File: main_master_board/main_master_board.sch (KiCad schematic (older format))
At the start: 4 parts, among them P5 Mounting Holes, P6 Mounting Holes, P7 Mounting Holes, P8 Mounting Holes

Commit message: Cleaned up some wires and moved connectors out to main page. Also added some LEDs
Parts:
- added D1, D2: D_Schottky, TO-220-3:D-Pack-3, symbol D_Schottky
- added D3: P6SMB30AT3G, Diodes_SMD:SMB_Standard, symbol ZENERsmall
- added F1: 3413.0328.22, dp_devices:dp_devices-C1206, symbol Fuse
- added P1: Hebi_1, Connectors_Molex:Molex_MiniFit-JR-5556-02A_2x01x4.20mm_Straight, symbol CONN_01X02
- added P13: CONN_02X15, symbol CONN_02X15
- added P2: Hebi_2, Connectors_Molex:Molex_MiniFit-JR-5556-02A_2x01x4.20mm_Straight, symbol CONN_01X02
- added P3: Vbackup, microclasp:microclasp_2, symbol CONN_01X02
- added P4: CONN_02X05, Connectors_Molex:Molex_NanoFit_2x05x2.50mm_Straight, symbol CONN_02X05
- added S1: SWITCH_DPDT, microclasp:microclasp_3, symbol SWITCH_DPDT
- added SW1: SWITCH_SPST, microclasp:microclasp_2, symbol SWITCH_SPST
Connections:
- net labels added: KS_physical_in, KS_physical_out, Switch_on, V24_in, V4, V_hebi1, V_hebi2, signal_1s, signal_2s, signal_3s, signal_4s, signal_5s, signal_6s, uC_GPIO1, uC_GPIO2
- net labels removed: +12V, +1V8, V12
- wire segments 79 -> 119
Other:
- note added: "Bettery Reverse\nCurrent Protection"
- note added: "Circuits can take 48V, \nexcept TSV diode"
- note added: "Manual switch to \nturn motors off"
- note added: "Molex Nano-Fit"
- note added: "Transient Voltage Suppessor"

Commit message: Started routing! 24 to 5 buck
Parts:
- D1, D2: footprint TO-220-3:D-Pack-3 -> PowerDI:PowerDI
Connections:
- wire segments 119 -> 111
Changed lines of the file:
@@
 LIBS:Sensors
 LIBS:LP3852-3.3
-LIBS:0s102011ma1qn1
-LIBS:74LVC1G17
-LIBS:74V1T126
-LIBS:acs711klctr-12ab-t
-LIBS:AD7192
-LIBS:AD7193
-LIBS:am-hrr30-xxx
-LIBS:aon7528
-LIBS:AP7363
-LIBS:AS1359
-LIBS:csd16323q3
-LIBS:dmn2004dmk
-LIBS:dp_devices
-LIBS:DSPIC33E128MC506
-LIBS:fds6898az
-LIBS:ina197
-LIBS:irf7329pbf
-LIBS:ld1117
-LIBS:lm3478
-LIBS:lm3481
-LIBS:lt1910
-LIBS:ltc1871
-LIBS:ltc1982
-LIBS:MAG3110
-LIBS:mcp1700
-LIBS:mcp73831
-LIBS:mcsmt-g5030a1-3712
-LIBS:microchip_can
-LIBS:microclasp_hdrx2
-LIBS:microclasp_hdrx3
-LIBS:MPU-6000_MPU-6050
-LIBS:MPU-9150
-LIBS:nrf24l01+
-LIBS:pds1040l
-LIBS:pic12f1571
-LIBS:pinhead
-LIBS:psmn013-80ys
-LIBS:RESISTOR_ARRAY
-LIBS:rf803d
-LIBS:RGB_LED
-LIBS:Si1970DH
-LIBS:sn65hvd232
-LIBS:ssc54
-LIBS:sw_push_4
-LIBS:tc74
-LIBS:TPS2113A
-LIBS:tps54540
-LIBS:vs-mbrb1635pbf
-LIBS:xal5050-562meb
-LIBS:xal6030-182mec
+LIBS:decaWave
 LIBS:conn_2x50
 LIBS:conn_open_q_x2
@@
 LIBS:ac-dc
 LIBS:actel
+LIBS:allegro
 LIBS:Altera
 LIBS:analog_devices
@@
 LIBS:logo
 LIBS:maxim
+LIBS:mechanical
 LIBS:microchip_dspic33dsc
 LIBS:microchip_pic10mcu
@@
 LIBS:microchip_pic32mcu
 LIBS:motor_drivers
+LIBS:motors
 LIBS:msp430
 LIBS:nordicsemi
@@
 LIBS:ttl_ieee
 LIBS:video
+LIBS:wiznet
 LIBS:Worldsemi
 LIBS:Xicor
+LIBS:zetex
 LIBS:Zilog
 LIBS:conn_2x45
@@
 Comment4 ""
 $EndDescr
-$Comp
-L +3V3 #PWR01
-U 1 1 58094C11
-P 1360 690
-F 0 "#PWR01" H 1360 540 50  0001 C CNN
-F 1 "+3V3" H 1360 830 50  0000 C CNN
-F 2 "" H 1360 690 50  0000 C CNN
-F 3 "" H 1360 690 50  0000 C CNN
-	1    1360 690
-	1    0    0    -1
-$EndComp
-$Comp
-L GND #PWR02
-U 1 1 58094D2E
-P 1250 1200
-F 0 "#PWR02" H 1250 950 50  0001 C CNN
-F 1 "GND" H 1250 1050 50  0000 C CNN
-F 2 "" H 1250 1200 50  0000 C CNN
-F 3 "" H 1250 1200 50  0000 C CNN
-	1    1250 1200
-	1    0    0    -1
-$EndComp
-$Comp
-L +24V #PWR03
-U 1 1 58643E79
-P 870 700
-F 0 "#PWR03" H 870 550 50  0001 C CNN
-F 1 "+24V" H 870 840 50  0000 C CNN
-F 2 "" H 870 700 50  0000 C CNN
-F 3 "" H 870 700 50  0000 C CNN
-	1    870  700
-	1    0    0    -1
-$EndComp
-$Comp
-L +5V #PWR04
-U 1 1 586440F8
-P 1120 690
-F 0 "#PWR04" H 1120 540 50  0001 C CNN
-F 1 "+5V" H 1120 830 50  0000 C CNN
-F 2 "" H 1120 690 50  0000 C CNN
-F 3 "" H 1120 690 50  0000 C CNN
-	1    1120 690
-	1    0    0    -1
-$EndComp
 $Sheet
 S 4700 860  1110 1660
@@
 Text Label 6965 1025 0    60   ~ 0
 Vmain
-$Comp
-L PWR_FLAG #FLG05
-U 1 1 58713441
-P 1120 1140
-F 0 "#FLG05" H 1120 1235 50  0001 C CNN
-F 1 "PWR_FLAG" H 1120 1320 50  0000 C CNN
-F 2 "" H 1120 1140 50  0000 C CNN
-F 3 "" H 1120 1140 50  0000 C CNN
-	1    1120 1140
-	1    0    0    -1
-$EndComp
-$Comp
-L PWR_FLAG #FLG06
-U 1 1 5871371D
-P 1120 790
-F 0 "#FLG06" H 1120 885 50  0001 C CNN
-F 1 "PWR_FLAG" H 1120 970 50  0001 C CNN
-F 2 "" H 1120 790 50  0000 C CNN
-F 3 "" H 1120 790 50  0000 C CNN
-	1    1120 790
-	-1   0    0    1
-$EndComp
-$Comp
-L GNDPWR #PWR07
-U 1 1 58714A82
-P 960 1200
-F 0 "#PWR07" H 960 1000 50  0001 C CNN
-F 1 "GNDPWR" H 960 1070 50  0000 C CNN
-F 2 "" H 960 1150 50  0000 C CNN
-F 3 "" H 960 1150 50  0000 C CNN
-	1    960  1200
-	1    0    0    -1
-$EndComp
-Text Notes 530  1580 0    60   ~ 0
+Text Notes 505  805  0    60   ~ 0
 Two Grounds to separate \nmotor ground and electronics ground
 Text Label 5850 1210 0    60   ~ 0
@@
 3V3
 $Comp
-L GNDPWR #PWR08
+L GNDPWR #PWR01
 U 1 1 58756896
 P 4460 2550
-F 0 "#PWR08" H 4460 2350 50  0001 C CNN
+F 0 "#PWR01" H 4460 2350 50  0001 C CNN
 F 1 "GNDPWR" H 4460 2420 50  0000 C CNN
 F 2 "" H 4460 2500 50  0000 C CNN
@@
 $EndComp
 $Comp
-L GND #PWR09
+L GND #PWR02
 U 1 1 58756928
 P 6030 2540
-F 0 "#PWR09" H 6030 2290 50  0001 C CNN
+F 0 "#PWR02" H 6030 2290 50  0001 C CNN
 F 1 "GND" H 6030 2390 50  0000 C CNN
 F 2 "" H 6030 2540 50  0000 C CNN
@@
 Vmotors
 $Comp
-L GND #PWR010
+L GND #PWR03
 U 1 1 5875B134
 P 7125 1915
-F 0 "#PWR010" H 7125 1665 50  0001 C CNN
+F 0 "#PWR03" H 7125 1665 50  0001 C CNN
 F 1 "GND" H 7125 1765 50  0000 C CNN
 F 2 "" H 7125 1915 50  0000 C CNN
@@
 $EndComp
 $Comp
-L GNDPWR #PWR011
+L GNDPWR #PWR04
 U 1 1 5875E5EF
 P 6875 1935
-F 0 "#PWR011" H 6875 1735 50  0001 C CNN
+F 0 "#PWR04" H 6875 1735 50  0001 C CNN
 F 1 "GNDPWR" H 6875 1805 50  0000 C CNN
 F 2 "" H 6875 1885 50  0000 C CNN
@@
 $EndSheet
 $Comp
-L GND #PWR012
+L GND #PWR05
 U 1 1 587B1461
 P 11140 940
-F 0 "#PWR012" H 11140 690 50  0001 C CNN
+F 0 "#PWR05" H 11140 690 50  0001 C CNN
 F 1 "GND" H 11140 790 50  0000 C CNN
 F 2 "" H 11140 940 50  0000 C CNN
@@
 prog_tx
 $Comp
-L GND #PWR013
+L GND #PWR06
 U 1 1 588455B7
 P 7955 6190
-F 0 "#PWR013" H 7955 5940 50  0001 C CNN
+F 0 "#PWR06" H 7955 5940 50  0001 C CNN
 F 1 "GND" H 7955 6040 50  0000 C CNN
 F 2 "" H 7955 6190 50  0000 C CNN
@@
 sensor_SCL
 Wire Wire Line
-	1120 690  1120 790
-Wire Wire Line
 	4700 1210 4150 1210
 Wire Wire Line
@@
 Wire Wire Line
 	6945 1025 7235 1025
-Wire Wire Line
-	870  700  870  750
-Wire Wire Line
-	870  750  1360 750
-Connection ~ 1120 750
-Wire Wire Line
-	1360 750  1360 690
-Wire Wire Line
-	960  1200 960  1140
-Wire Wire Line
-	960  1140 1250 1140
-Wire Wire Line
-	1250 1140 1250 1200
-Connection ~ 1120 1140
 Wire Wire Line
 	5810 1210 6075 1210
@@
 	5675 4860 6225 4860
 $Comp
-L GND #PWR014
+L GND #PWR07
 U 1 1 5889E95F
 P 4125 5785
-F 0 "#PWR014" H 4125 5535 50  0001 C CNN
+F 0 "#PWR07" H 4125 5535 50  0001 C CNN
 F 1 "GND" H 4125 5635 50  0000 C CNN
 F 2 "" H 4125 5785 50  0000 C CNN
@@
 Vbackup_in
 $Comp
-L GND #PWR015
+L GND #PWR08
 U 1 1 588D5080
 P 1480 5060
-F 0 "#PWR015" H 1480 4810 50  0001 C CNN
+F 0 "#PWR08" H 1480 4810 50  0001 C CNN
 F 1 "GND" H 1480 4910 50  0000 C CNN
 F 2 "" H 1480 5060 50  0000 C CNN
@@
 V_hebi1
 $Comp
-L GNDPWR #PWR016
+L GNDPWR #PWR09
 U 1 1 588D5095
 P 1185 5830
-F 0 "#PWR016" H 1185 5630 50  0001 C CNN
+F 0 "#PWR09" H 1185 5630 50  0001 C CNN
 F 1 "GNDPWR" H 1185 5700 50  0000 C CNN
 F 2 "" H 1185 5780 50  0000 C CNN
@@
 $EndComp
 $Comp
-L GNDPWR #PWR017
+L GNDPWR #PWR010
 U 1 1 588D509B
 P 1175 6270
-F 0 "#PWR017" H 1175 6070 50  0001 C CNN
+F 0 "#PWR010" H 1175 6070 50  0001 C CNN
 F 1 "GNDPWR" H 1175 6140 50  0000 C CNN
 F 2 "" H 1175 6220 50  0000 C CNN
@@
 F 0 "D2" H 1135 7050 50  0000 C CNN
 F 1 "D_Schottky" H 1135 6850 50  0000 C CNN
-F 2 "TO-220-3:D-Pack-3" H 1135 6950 50  0001 C CNN
+F 2 "PowerDI:PowerDI" H 1135 6950 50  0001 C CNN
 F 3 "http://datasheet.octopart.com/STPS5H100B-TR-STMicroelectronics-datasheet-5318140.pdf" H 1135 6950 50  0001 C CNN
 	1    1135 6950
@@
 F 0 "D1" H 1125 7340 50  0000 C CNN
 F 1 "D_Schottky" H 1125 7140 50  0000 C CNN
-F 2 "TO-220-3:D-Pack-3" H 1125 7240 50  0001 C CNN
+F 2 "PowerDI:PowerDI" H 1125 7240 50  0001 C CNN
 F 3 "http://datasheet.octopart.com/STPS5H100B-TR-STMicroelectronics-datasheet-5318140.pdf" H 1125 7240 50  0001 C CNN
 	1    1125 7240
@@
 	1190 3790 1190 3820
 $Comp
-L GNDPWR #PWR018
+L GNDPWR #PWR011
 U 1 1 588D5126
 P 1190 3820
-F 0 "#PWR018" H 1190 3620 50  0001 C CNN
+F 0 "#PWR011" H 1190 3620 50  0001 C CNN
 F 1 "GNDPWR" H 1190 3690 50  0000 C CNN
 F 2 "" H 1190 3770 50  0000 C CNN
@@
 $EndComp
 $Comp
-L GNDPWR #PWR019
+L GNDPWR #PWR012
 U 1 1 588D512C
 P 2030 4420
-F 0 "#PWR019" H 2030 4220 50  0001 C CNN
+F 0 "#PWR012" H 2030 4220 50  0001 C CNN
 F 1 "GNDPWR" H 2030 4290 50  0000 C CNN
 F 2 "" H 2030 4370 50  0000 C CNN
@@
 	8555 1310 9330 1310
 $Comp
-L GNDPWR #PWR020
+L GNDPWR #PWR013
 U 1 1 588EACE1
 P 1320 2845
-F 0 "#PWR020" H 1320 2645 50  0001 C CNN
+F 0 "#PWR013" H 1320 2645 50  0001 C CNN
 F 1 "GNDPWR" H 1320 2715 50  0000 C CNN
 F 2 "" H 1320 2795 50  0000 C CNN
@@
 V4
 $Comp
-L +24V #PWR021
+L +24V #PWR014
 U 1 1 58919C55
 P 4300 900
-F 0 "#PWR021" H 4300 750 50  0001 C CNN
+F 0 "#PWR014" H 4300 750 50  0001 C CNN
 F 1 "+24V" H 4300 1040 50  0000 C CNN
 F 2 "" H 4300 900 50  0000 C CNN
@@
 Switch_on
 $Comp
-L +5V #PWR022
+L +5V #PWR015
 U 1 1 58924C9E
 P 6075 1175
-F 0 "#PWR022" H 6075 1025 50  0001 C CNN
+F 0 "#PWR015" H 6075 1025 50  0001 C CNN
 F 1 "+5V" H 6075 1315 50  0000 C CNN
 F 2 "" H 6075 1175 50  0000 C CNN
@@
 $EndComp
 $Comp
-L +3V3 #PWR023
+L +3V3 #PWR016
 U 1 1 58925954
 P 6075 1425
-F 0 "#PWR023" H 6075 1275 50  0001 C CNN
+F 0 "#PWR016" H 6075 1275 50  0001 C CNN
 F 1 "+3V3" H 6075 1565 50  0000 C CNN
 F 2 "" H 6075 1425 50  0000 C CNN
@@
 Wire Wire Line
 	6075 1460 6075 1425
-$Comp
-L +24V #PWR024
-U 1 1 5892EF1B
-P 600 2425
-F 0 "#PWR024" H 600 2275 50  0001 C CNN
-F 1 "+24V" H 600 2565 50  0000 C CNN
-F 2 "" H 600 2425 50  0000 C CNN
-F 3 "" H 600 2425 50  0000 C CNN
-	1    600  2425
-	1    0    0    -1
-$EndComp
-Wire Wire Line
-	600  2545 600  2425
 $EndSCHEMATC

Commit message: Routing power. Added 5V leveling cap.
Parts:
- removed P13: CONN_02X15, symbol CONN_02X15
- added P13: CONN_02X20, Hirose:DF40HC(3.0)-40DS-0.4V(51), symbol CONN_02X20
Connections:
- net labels added: 1V8, I2C1_SCL, I2C1_SDA, PRTCTL2, PRTCTL3, RB11, RB12, RD1, RD2, RD3, RD4, RD5, RD9, RE5, RF2, RF3, RF4, RF5, RF6, SDC2_CLK, SDC2_CMD, SDC2_DATA_0, SDC2_DATA_1, SDC2_DATA_2, SDC2_DATA_3, UART0_CTS_N, UART0_RTS_N, UART0_RX, UART0_TX, USBDM2, USBDM3, USBDP2, USBDP3, VREG_L11_SDC
- wire segments 111 -> 190
- no-connect marks 0 -> 1
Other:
- moved on the sheet: S1A, SW1

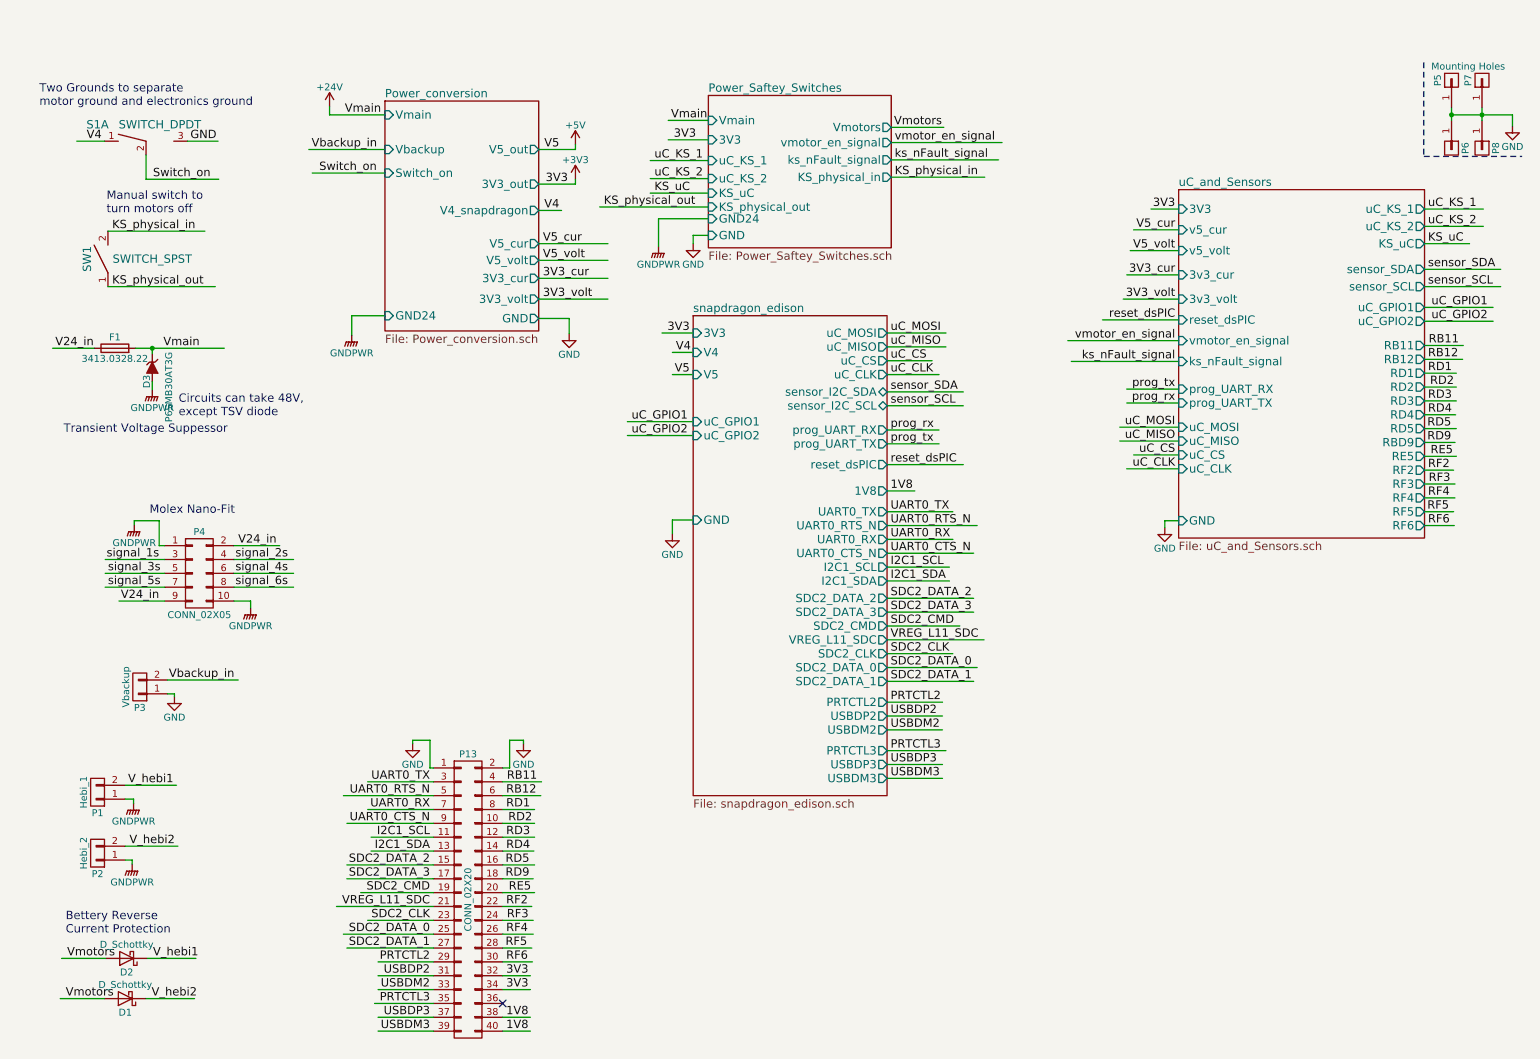
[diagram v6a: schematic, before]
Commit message: Addind support for a push button start and stop
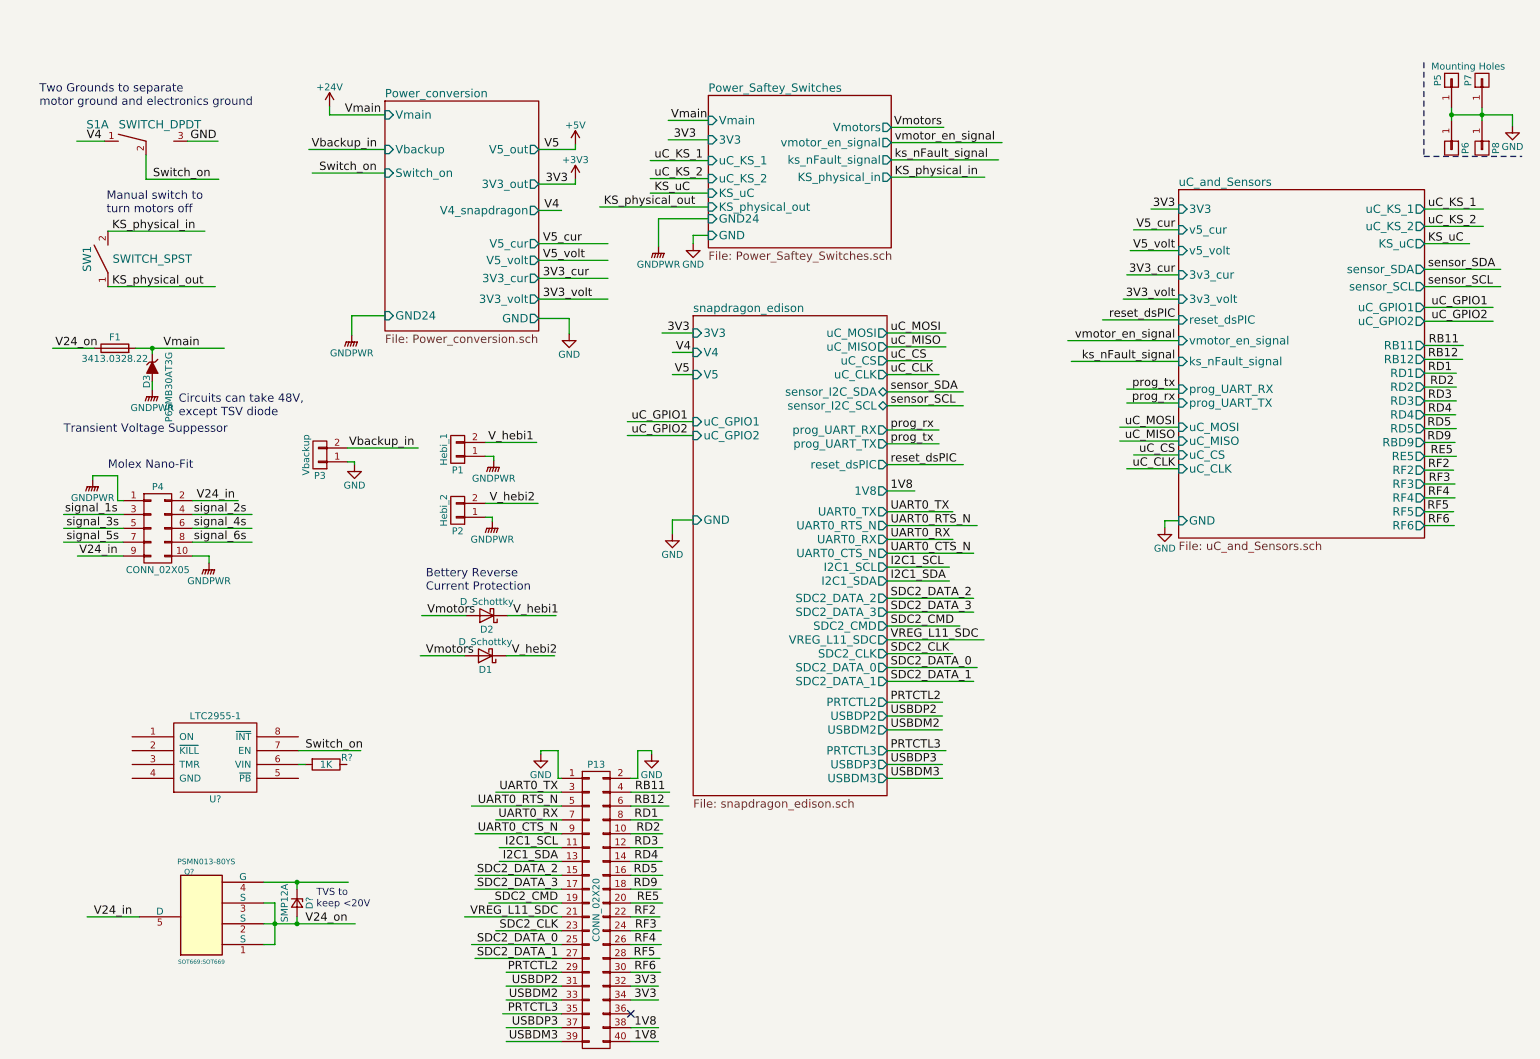
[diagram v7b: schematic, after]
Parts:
- added D?: SMP12A, DO-220AA:DO-220AA, symbol D_Zener_Small
- added Q?: PSMN013-80YS, SOT669:SOT669, symbol PSMN013-80YS
- added R?: 1K, symbol R
- added U?: LTC2955-1, MODULE, symbol LTC2955-1
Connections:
- net labels added: V24_on
- wire segments 190 -> 208
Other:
- note added: "TVS to \nkeep <20V"
- moved on the sheet: D1, D2, P1, P13, P2, P3, P4

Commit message: Working on routing near n-p mosfets. save point incase new apporach doesn't work out
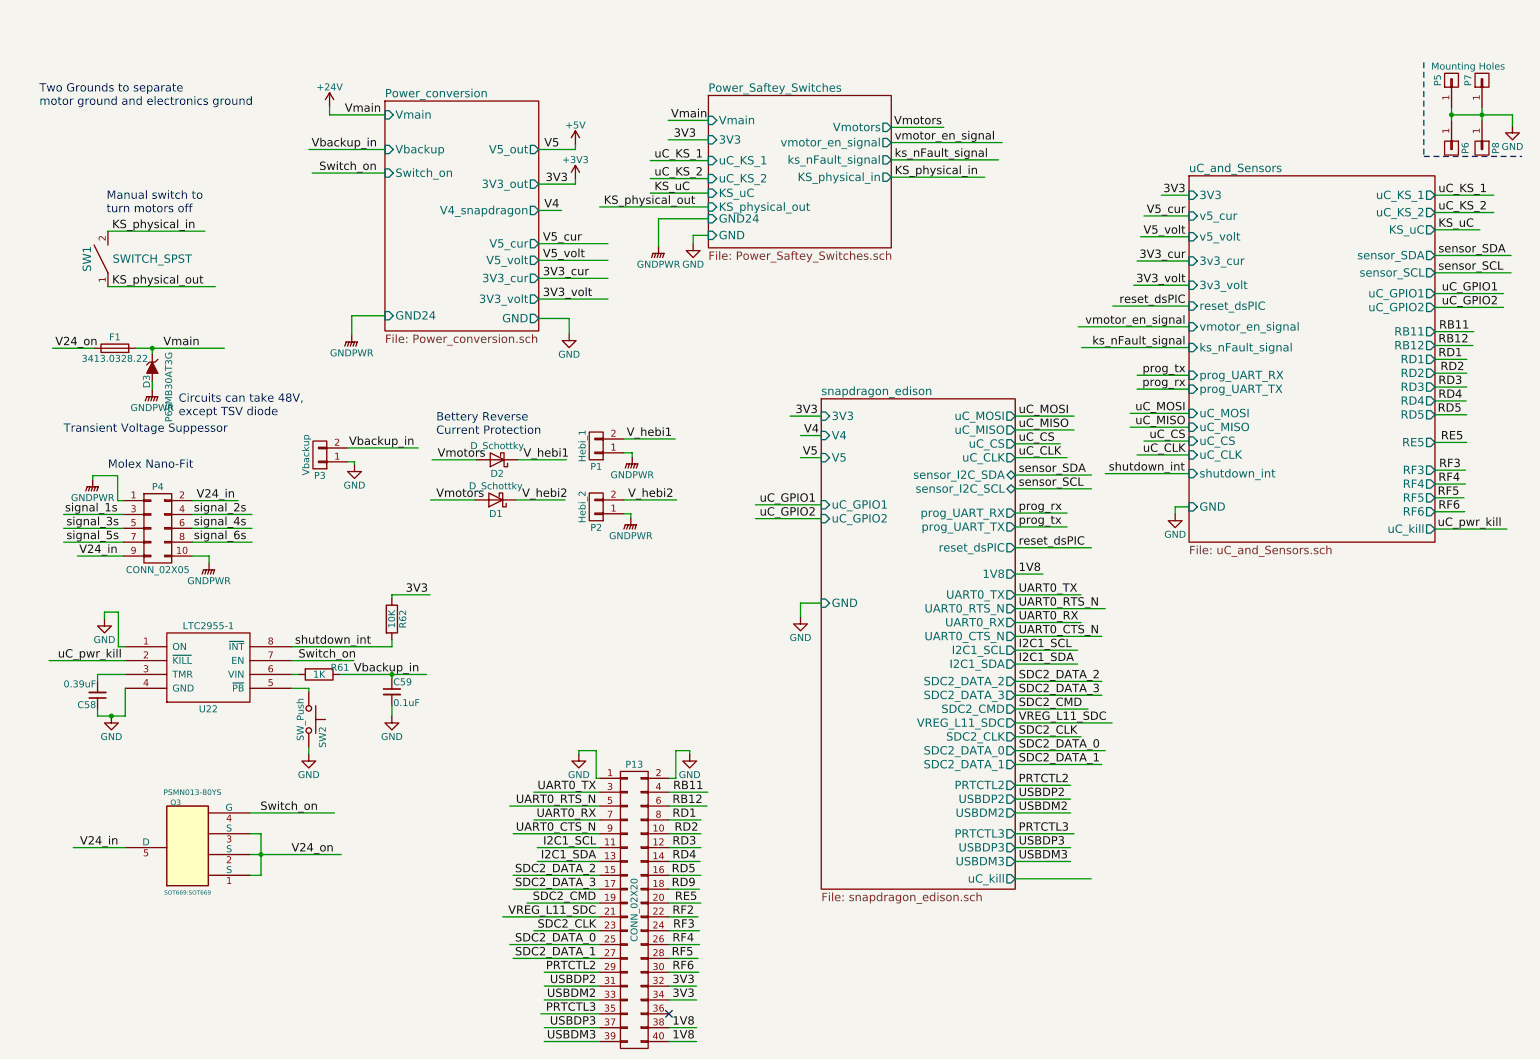
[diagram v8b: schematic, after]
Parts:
- removed D?: SMP12A, DO-220AA:DO-220AA, symbol D_Zener_Small
- removed S1: SWITCH_DPDT, microclasp:microclasp_3, symbol SWITCH_DPDT
- added C58: 0.39uF, Capacitors_SMD:C_0402, symbol C_Small
- added C59: 0.1uF, Capacitors_SMD:C_0402, symbol C_Small
- added R62: 10K, Resistors_SMD:R_0402, symbol R
- added SW2: SW_Push, microclasp:microclasp_2, symbol SW_Push
- R61: renamed from R?; footprint (none) -> Resistors_SMD:R_0402
- U22: renamed from U?; footprint MODULE -> TSOT-23:TSOT-23-8
- gave numbers to parts that had none: 1
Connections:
- net labels added: shutdown_int, uC_pwr_kill
- wire segments 208 -> 215
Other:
- note removed: "TVS to \nkeep <20V"
- moved on the sheet: D1, D2, P1, P13, P2, Q3, R61, U22
